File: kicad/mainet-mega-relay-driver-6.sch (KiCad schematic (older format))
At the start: 8 parts, among them J35 Screw_Terminal_01x03, K6 SANYOU_SRD_Form_C, Q6 2N3904, U7 4N37

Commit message: KICAD: Actualizar archivos del módulo de relés
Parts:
- added J89, J90: Conn_01x01_Male, symbol Connector:Conn_01x01_Male
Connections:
- net C6 renamed clutchChunkActivation
- net clutchChunkActivation: now also J90.1 (Pin_1)
- net NO6 renamed +24V
- net +24V: now also J89.1 (Pin_1)
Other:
- note added: "Activación de la válvula solenoide,\n2 posiciones simple,\nde los "chunk" de los embragues\n"
- note added: "JD-VCC:\n\nFuente externa de +5V\n(No es la salida de +5V \ndel Arduino)"
- note added: "Relay Ground\nNo conectar a la tierra\ndel Arduino Mega\n"
- note added: "VCC:\n\nSalida +5V del Arduino"
- note removed: "JD-VCC:\nFuente externa de +5V\n(No es la salida de +5V \ndel Arduino)"
- note removed: "No conectar a la tierra del Arduino Mega\n"
- note removed: "Relay Ground\n"
- note removed: "VCC:\nSalida +5V del Arduino"
- moved on the sheet: D11, D12, J35, K6, Q6, R11, R12, U7

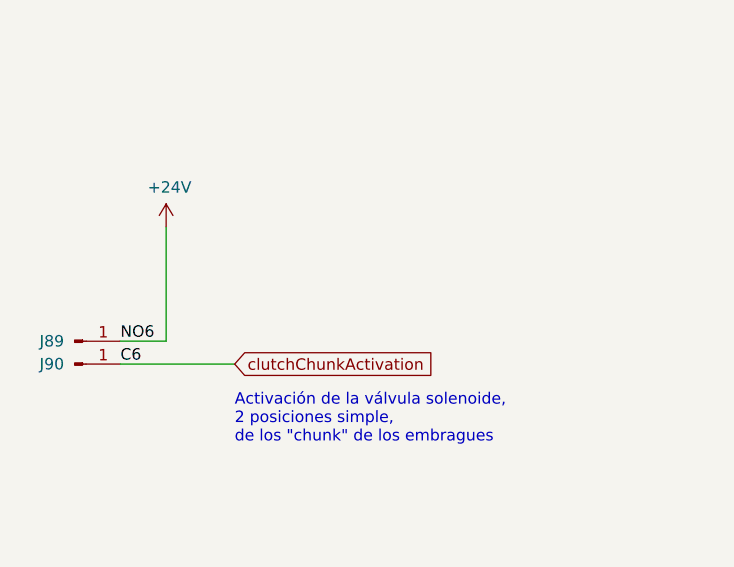
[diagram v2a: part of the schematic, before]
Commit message: KICAD: Agregar cambios esquemáticos
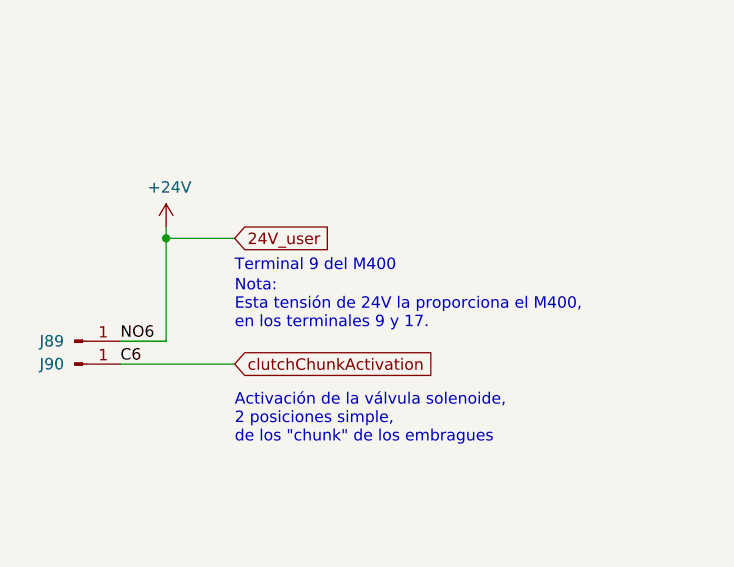
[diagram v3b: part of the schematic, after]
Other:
- note added: "Nota:\nEsta tensión de 24V la proporciona el M400, \nen los terminales 9 y 17."
- note added: "Terminal 9 del M400"
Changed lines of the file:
@@
 Sheet 12 22
 Title "Mainet-mega -- clutchChunkControl"
-Date "2021-06-17"
+Date "2021-06-18"
 Rev "1.0"
 Comp "Tovenca"
@@
 $EndComp
 Wire Wire Line
-	8700 3250 8700 3750
+	8700 3250 8700 3300
 Wire Wire Line
 	8700 3750 8500 3750
@@
 Text GLabel 5250 1650 2    50   Input ~ 0
 clutchChunkActivation
+Text GLabel 9000 3300 2    50   Input ~ 0
+24V_user
+Wire Wire Line
+	8700 3300 9000 3300
+Text Notes 9000 3450 0    50   ~ 0
+Terminal 9 del M400
+Text Notes 9000 3700 0    50   ~ 0
+Nota:\nEsta tensión de 24V la proporciona el M400, \nen los terminales 9 y 17.
+Connection ~ 8700 3300
+Wire Wire Line
+	8700 3300 8700 3750
 $EndSCHEMATC

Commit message: KICAD: Actualizar .sch chuck embrague inferior
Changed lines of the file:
@@
 Sheet 12 22
 Title "Mainet-mega -- clutchChunkControl"
-Date "2021-06-18"
+Date "2021-07-14"
 Rev "1.0"
 Comp "Tovenca"
@@
 clutchChunkActivation
 Text GLabel 9000 3300 2    50   Input ~ 0
-24V_user
++24V
 Wire Wire Line
 	8700 3300 9000 3300
